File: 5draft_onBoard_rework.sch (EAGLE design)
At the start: 69 parts, among them IC3 74ABT125PW, IC4 MAX4466KS, J2 USB_MINI-B_DIGIKEY, Q1 NPN 40V 1A SOT-23

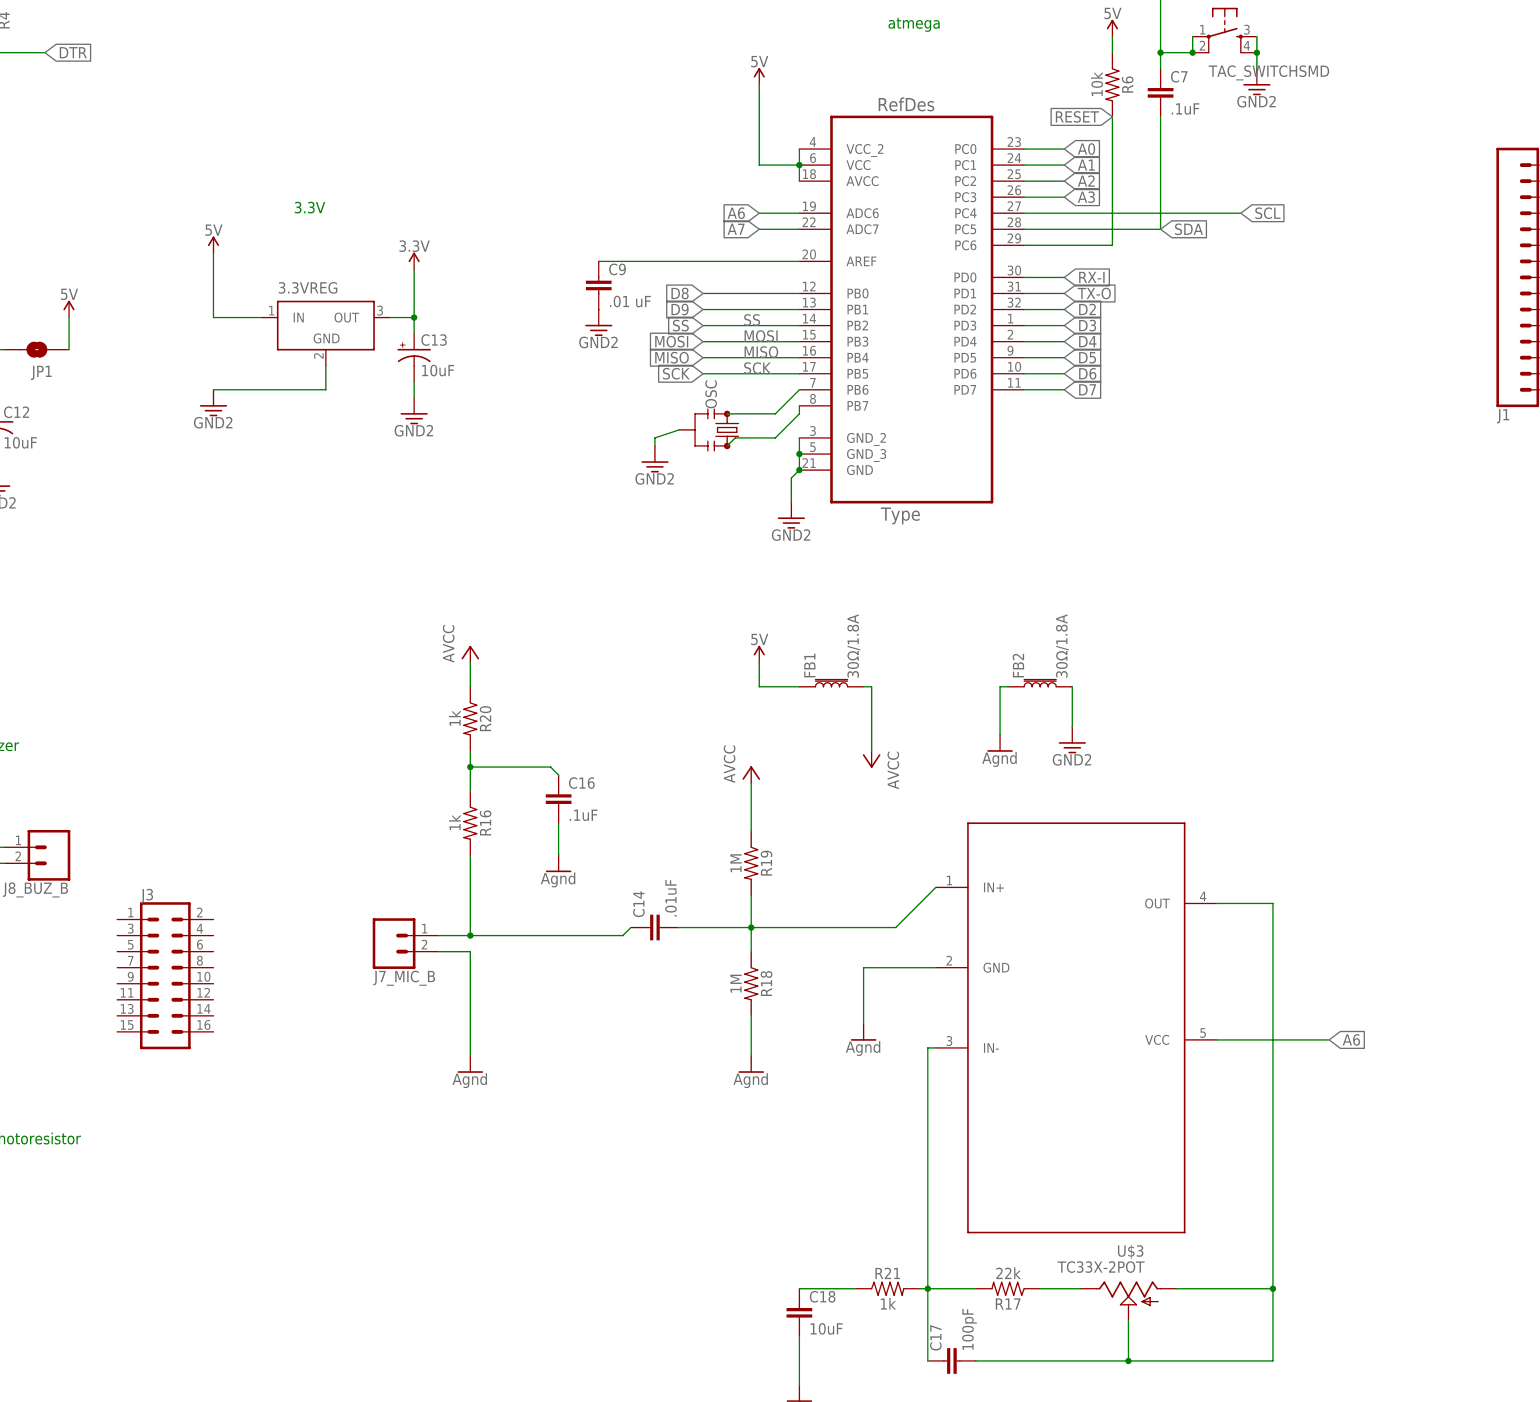
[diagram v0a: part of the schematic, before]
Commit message: re arranging nano layout
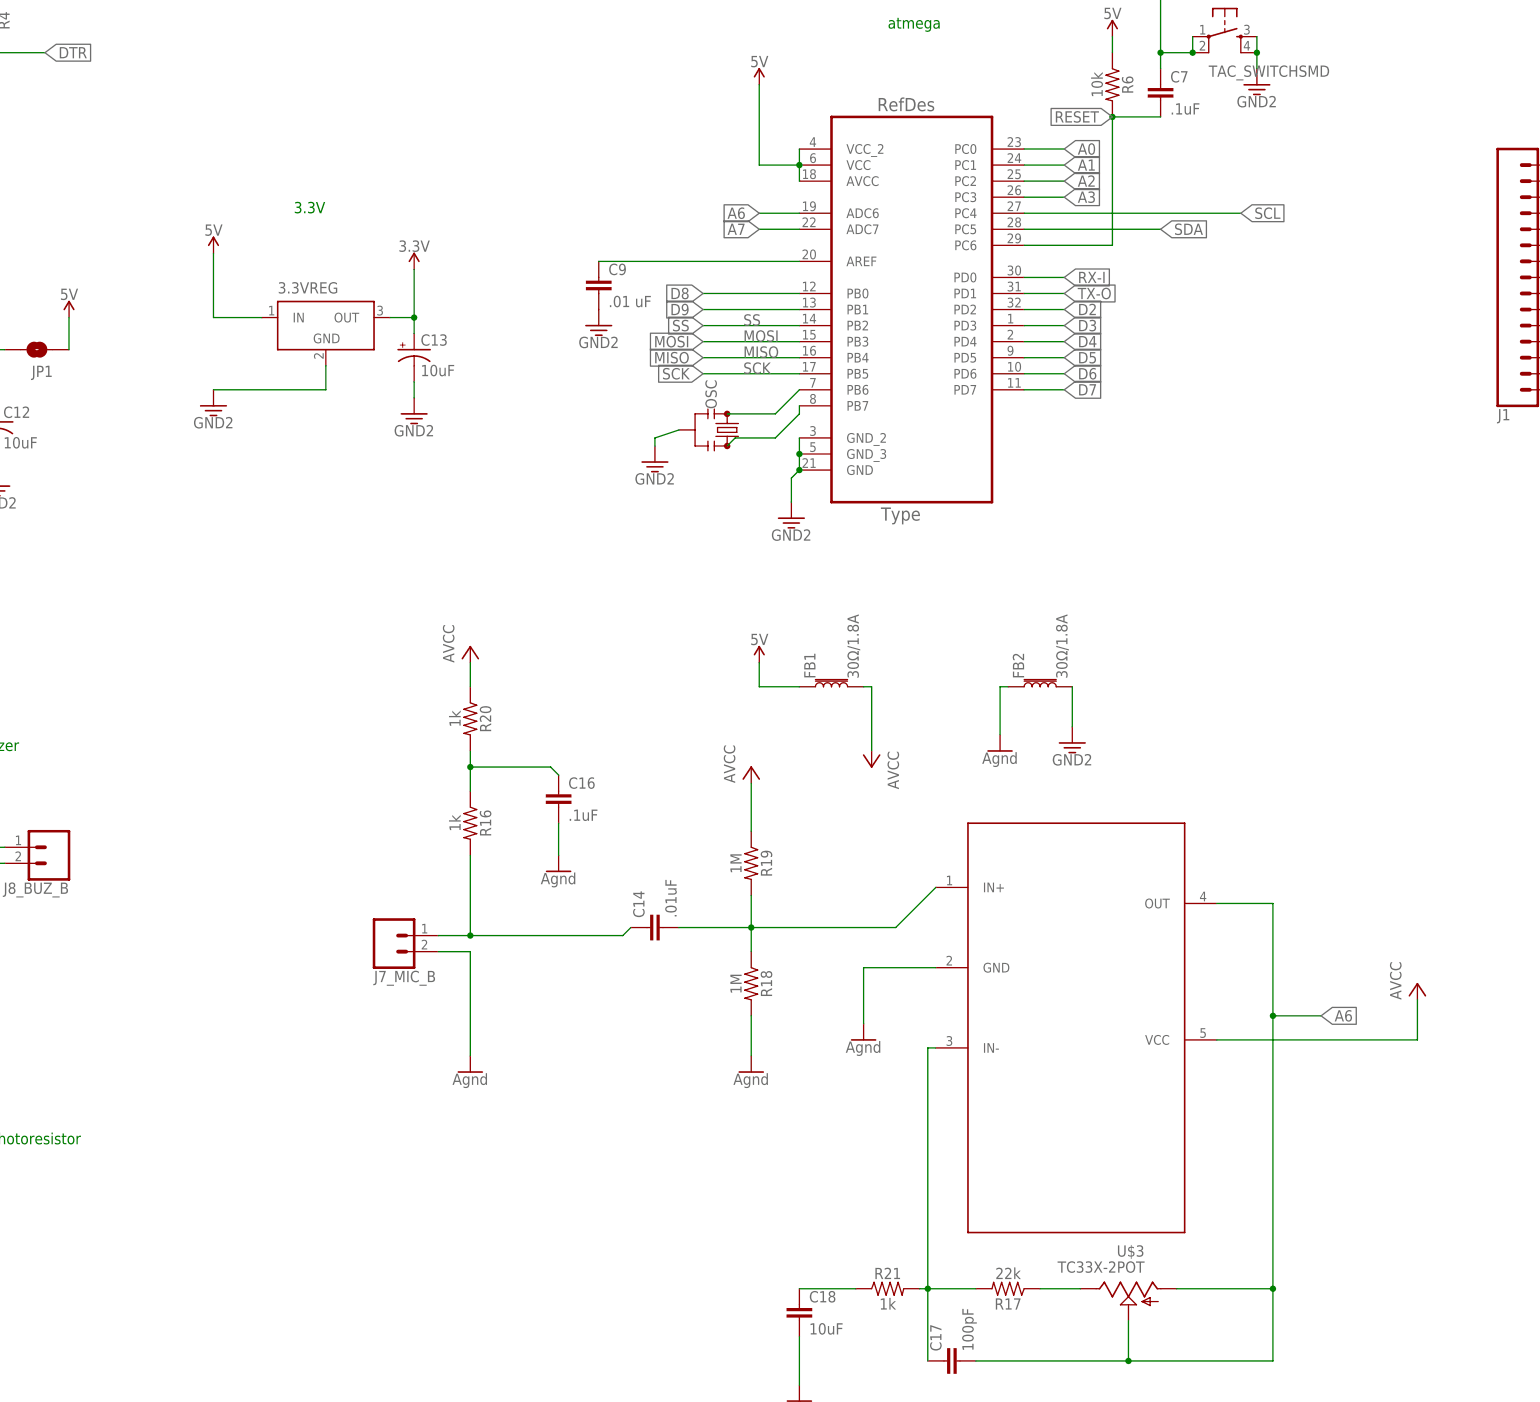
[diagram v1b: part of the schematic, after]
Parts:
- removed J3: (no value), SparkFun-Connectors:CONN_08X2
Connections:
- net D+ renamed D+_P
- net D- renamed D-_N
- net N$1 renamed PB6
- net N$14 renamed USBDP_N
- net N$15 renamed USBDM_P
- net N$2 renamed PB7
- removed net N$32: C17.2, IC4.OUT, U$3.2, U$3.3
- removed net VCC: C11.+, FB1.2, FB3.2, FTDI231XS1.VCC, R19.1, R20.1
- new net AVCC: FB1.2, IC4.VCC, R19.1, R20.1
- net 5V: now also C11.+, FB3.2, FTDI231XS1.VCC
- net A6: now also C17.2, IC4.OUT, U$3.2, U$3.3; no longer IC4.VCC
- net RESET: now also C7.2
- net SDA: no longer C7.2

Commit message: removed 3.3v and changed buffer to be 5v
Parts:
- removed 3.3VREG: (no value), linear-technology:LT1129CST5
- removed C13: 10uF, SparkFun-Retired:10UF-TANT
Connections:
- removed net 3.3V: 3.3VREGG$1.OUT, C13.+, IC3D.I, IC3D.O, IC3D.OE, R14.1, U$2.VDD
- net 5V: now also IC3D.I, IC3D.O, IC3D.OE, R14.1, U$2.VDD; no longer 3.3VREGG$1.IN
- net GND: no longer 3.3VREGG$1.GND, C13.-
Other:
- note removed: "3.3V"

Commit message: adding pir sensors to board
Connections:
- removed net USBDP_N: FTDI231XS1.USBDP, R7.2
- new net N$1: FTDI231XS1.USBDM, R7.2
- net USBDM_P: now also FTDI231XS1.USBDP; no longer FTDI231XS1.USBDM
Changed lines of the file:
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@@
 <setting verticaltext="up"/>
 </settings>
-<grid distance="0.05" unitdist="inch" unit="inch" style="lines" multiple="1" display="no" altdistance="0.005" altunitdist="inch" altunit="inch"/>
+<grid distance="0.1" unitdist="inch" unit="inch" style="lines" multiple="1" display="no" altdistance="0.01" altunitdist="inch" altunit="inch"/>
 <layers>
 <layer number="1" name="Top" color="4" fill="1" visible="no" active="no"/>
@@
 </segment>
 </net>
-<net name="USBDP_N" class="0">
-<segment>
-<pinref part="R7" gate="G$1" pin="2"/>
-<pinref part="FTDI231XS1" gate="U$1" pin="USBDP"/>
-<wire x1="-582.93" y1="130.81" x2="-554.99" y2="130.81" width="0.1524" layer="91"/>
-<wire x1="-554.99" y1="130.81" x2="-544.83" y2="134.62" width="0.1524" layer="91"/>
-</segment>
-</net>
 <net name="USBDM_P" class="0">
 <segment>
 <pinref part="R5" gate="G$1" pin="2"/>
 <wire x1="-570.23" y1="133.35" x2="-554.99" y2="133.35" width="0.1524" layer="91"/>
-<pinref part="FTDI231XS1" gate="U$1" pin="USBDM"/>
-<wire x1="-554.99" y1="133.35" x2="-544.83" y2="137.16" width="0.1524" layer="91"/>
+<pinref part="FTDI231XS1" gate="U$1" pin="USBDP"/>
+<wire x1="-544.83" y1="134.62" x2="-554.99" y2="134.62" width="0.1524" layer="91"/>
+<wire x1="-554.99" y1="134.62" x2="-554.99" y2="133.35" width="0.1524" layer="91"/>
 </segment>
 </net>
@@
 </segment>
 </net>
+<net name="N$1" class="0">
+<segment>
+<pinref part="R7" gate="G$1" pin="2"/>
+<wire x1="-582.93" y1="130.81" x2="-558.8" y2="130.81" width="0.1524" layer="91"/>
+<wire x1="-558.8" y1="130.81" x2="-558.8" y2="137.16" width="0.1524" layer="91"/>
+<pinref part="FTDI231XS1" gate="U$1" pin="USBDM"/>
+<wire x1="-558.8" y1="137.16" x2="-544.83" y2="137.16" width="0.1524" layer="91"/>
+</segment>
+</net>

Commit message: redoing layout, condensing.
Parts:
- added J9_PIR1, J9_PIR2, J9_PIR3: (no value), SparkFun-Connectors:CONN_03
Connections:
- net N$1 renamed USBDM_N
- new net VUSB: C11.+, C5.1, FB3.1, FB3.2, FTDI231XS1.VCC, J2.VBUS
- net 5V: now also J9_PIR1.2, J9_PIR2.2, J9_PIR3.2; no longer C11.+, C5.1, FB3.1, FB3.2, FTDI231XS1.VCC, J2.VBUS
- net D4: now also J9_PIR2.1
- net D7: now also J9_PIR1.1
- net D8: now also J9_PIR3.1
- net GND: now also J9_PIR1.3, J9_PIR2.3, J9_PIR3.3
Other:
- note added: "PIR1"
- moved on the sheet: J2
